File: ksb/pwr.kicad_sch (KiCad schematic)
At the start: 111 parts, among them Q1 Q_NMOS, U4 X850744-001

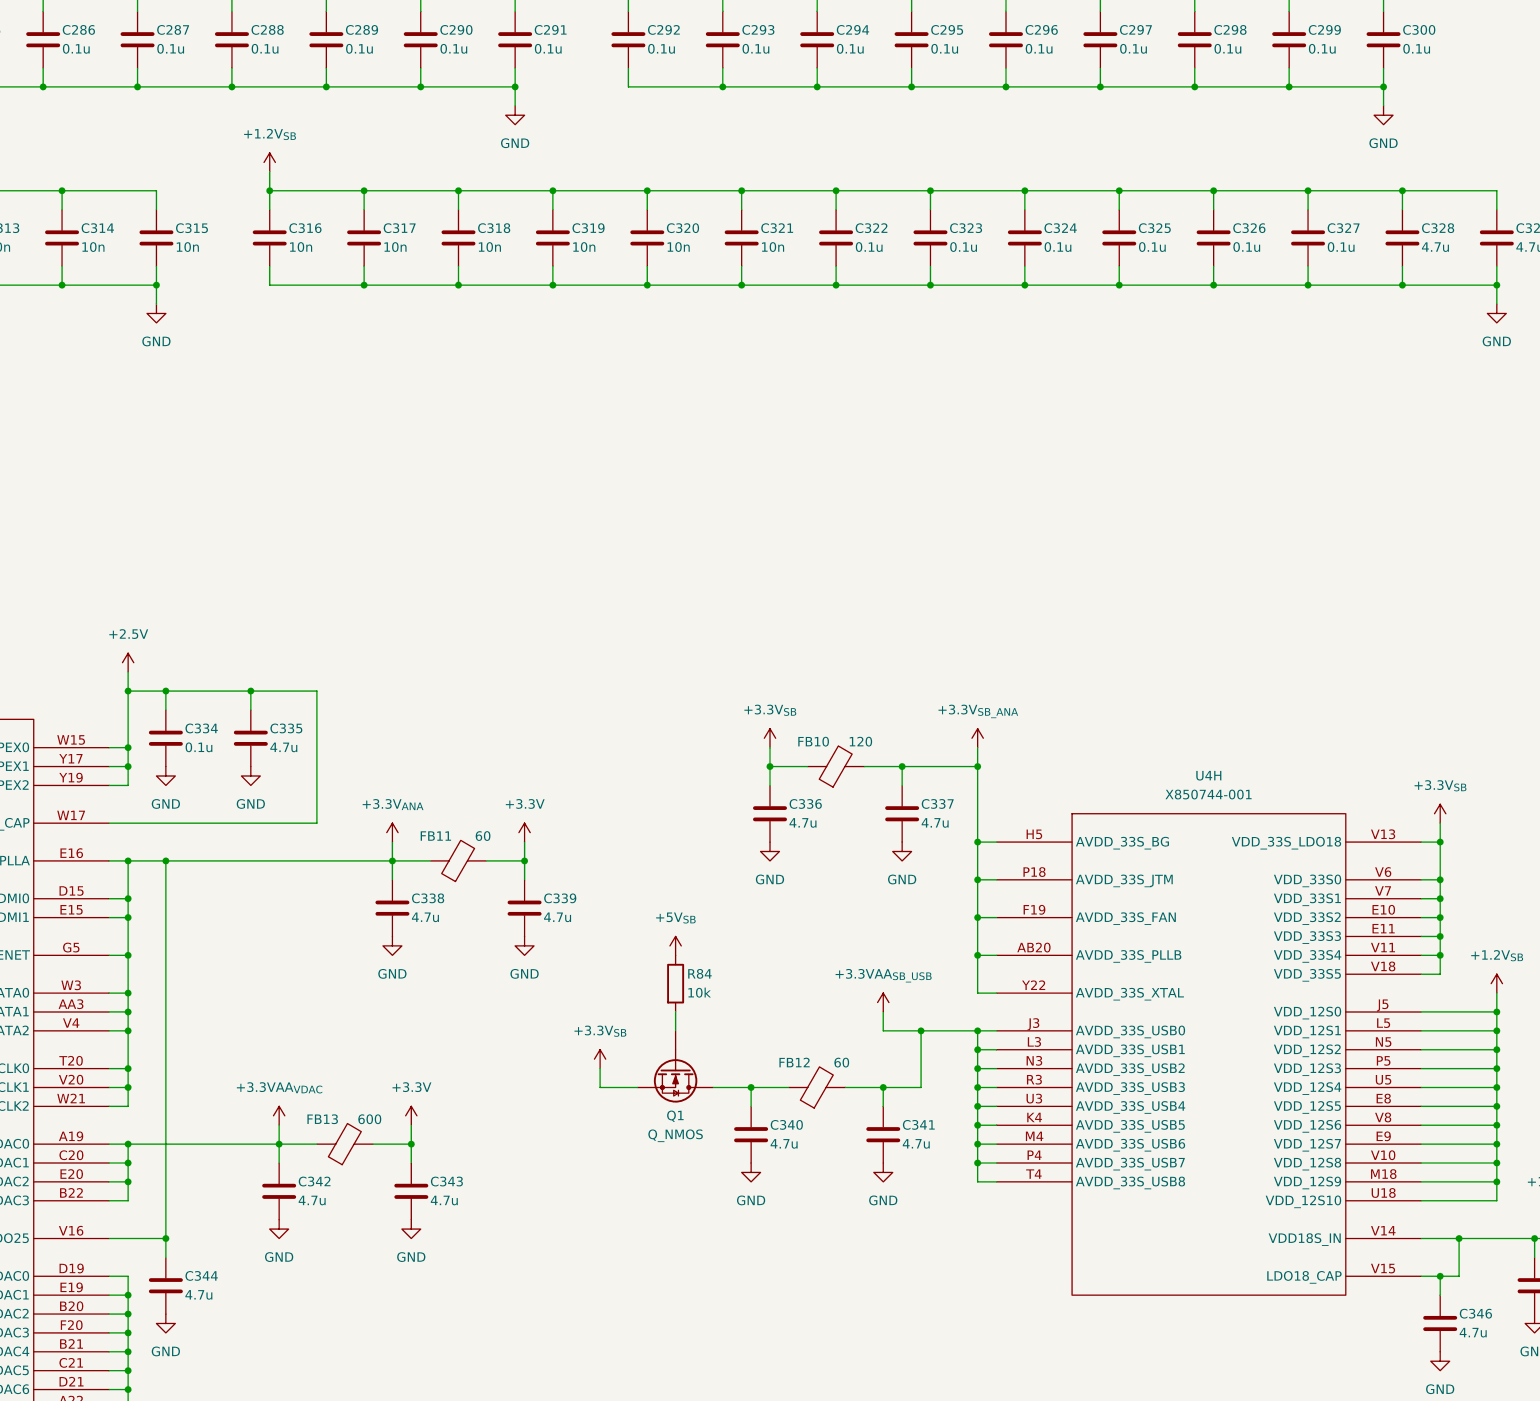
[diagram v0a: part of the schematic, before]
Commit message: Audio Output, Analog isolation and TOSLINK
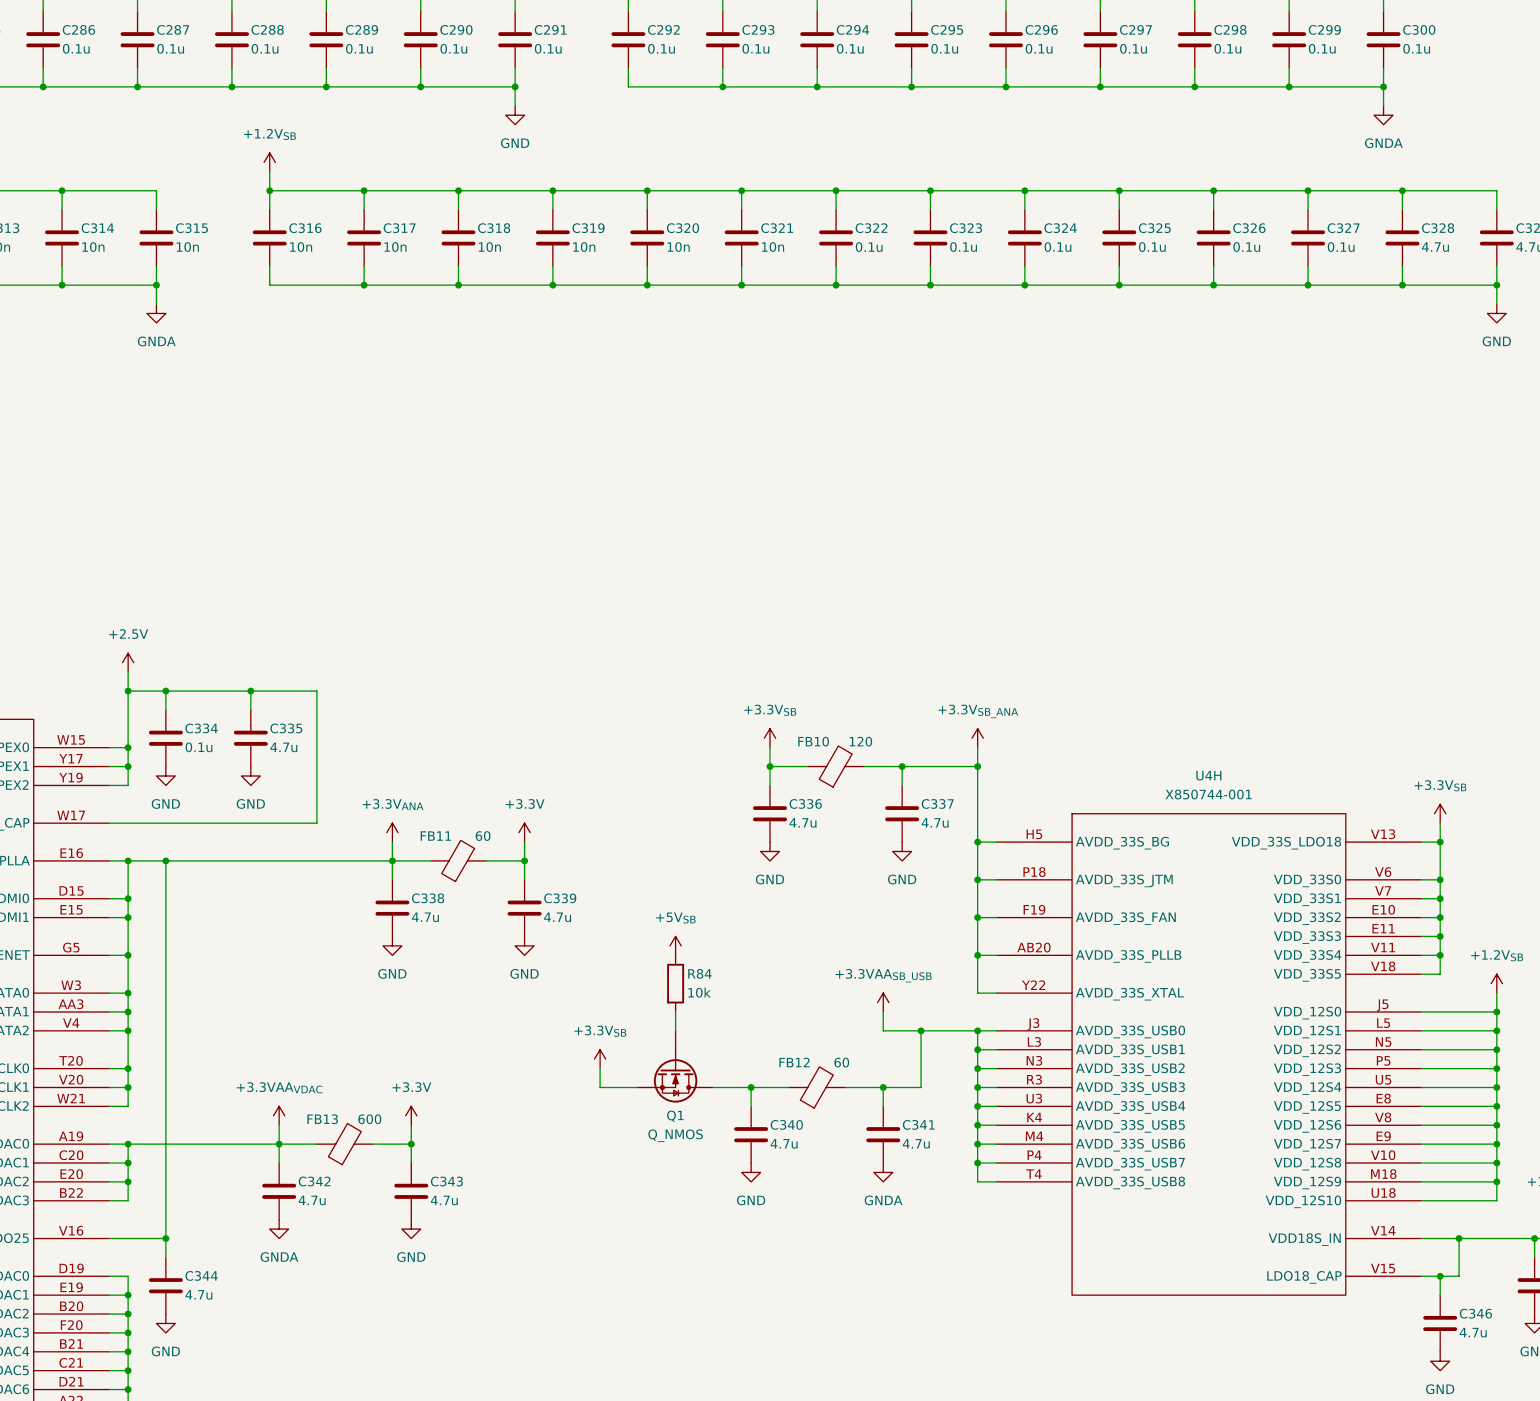
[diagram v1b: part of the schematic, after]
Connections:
- net GND: no longer C292.2, C293.2, C294.2, C295.2, C296.2, C297.2, C298.2, C299.2, C300.2, C312.2, C313.2, C314.2, C315.2, C341.2, C342.2
- new net GNDA: C292.2, C293.2, C294.2, C295.2, C296.2, C297.2, C298.2, C299.2, C300.2, C312.2, C313.2, C314.2, C315.2, C341.2, C342.2

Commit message: Multipurpose and standby power rails, Reannotated schematic
Added V_1P2, V_1P8, V_5P0DUAL, V_EFUSE, V_GPUPCIE, V_3P3STBY and V_1P2STBY
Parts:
- renumbered C244 to C239, C273 to C240, C301 to C241, C330 to C242, C245 to C243, C274 to C244, C302 to C245, C331 to C246, C246 to C247, C275 to C248, C303 to C249, C247 to C250, C276 to C251, C304 to C252, C248 to C253, C277 to C254, C305 to C255, C249 to C256, C278 to C257, C306 to C258, C250 to C259, C279 to C260, C307 to C261, C251 to C262, C280 to C263, C332 to C264, C308 to C265, C252 to C266, C281 to C267, C309 to C268, C333 to C269, C253 to C270, C282 to C271, C310 to C272, C254 to C273, C283 to C274, C311 to C275, C255 to C276, C284 to C277, C312 to C278, C256 to C279, C285 to C280, C313 to C281, C257 to C282, C286 to C283, C314 to C284, C258 to C285, C287 to C286, C315 to C287, C334 to C288, C344 to C289, C259 to C290, C288 to C291, C335 to C292, C316 to C293, C342 to C294, C260 to C295, C289 to C296, C317 to C297, C338 to C298, C343 to C299, C261 to C300, C290 to C301, C318 to C302, C262 to C303, C291 to C304, C339 to C305, C319 to C306, C263 to C307, C292 to C308, C320 to C309, C264 to C310, C293 to C311, C321 to C312, C340 to C313, C336 to C314, C265 to C315, C294 to C316, C322 to C317, C341 to C318, C266 to C319, C337 to C320, C295 to C321, C323 to C322, C267 to C323, C296 to C324, C324 to C325, C268 to C326, C297 to C327, C325 to C328, C269 to C329, C298 to C330, C326 to C331, C270 to C332, C299 to C333, C327 to C334, C271 to C335, C300 to C336, C328 to C337, C346 to C338, C272 to C339, C329 to C340, C345 to C341, FB13 to FB10, FB10 to FB13, Q1 to Q2, R84 to R85, U4 to U5
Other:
- moved on the sheet: C264, C269, C288, C289, C292, C294, C298, C299, C305, C313, C314, C318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
